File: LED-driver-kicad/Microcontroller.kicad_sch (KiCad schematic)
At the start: 11 parts, among them J2 Conn_01x05_Socket, J3 Conn_01x02_Socket, SW1 SW_SPDT, U5 PIC16F18026-ISL

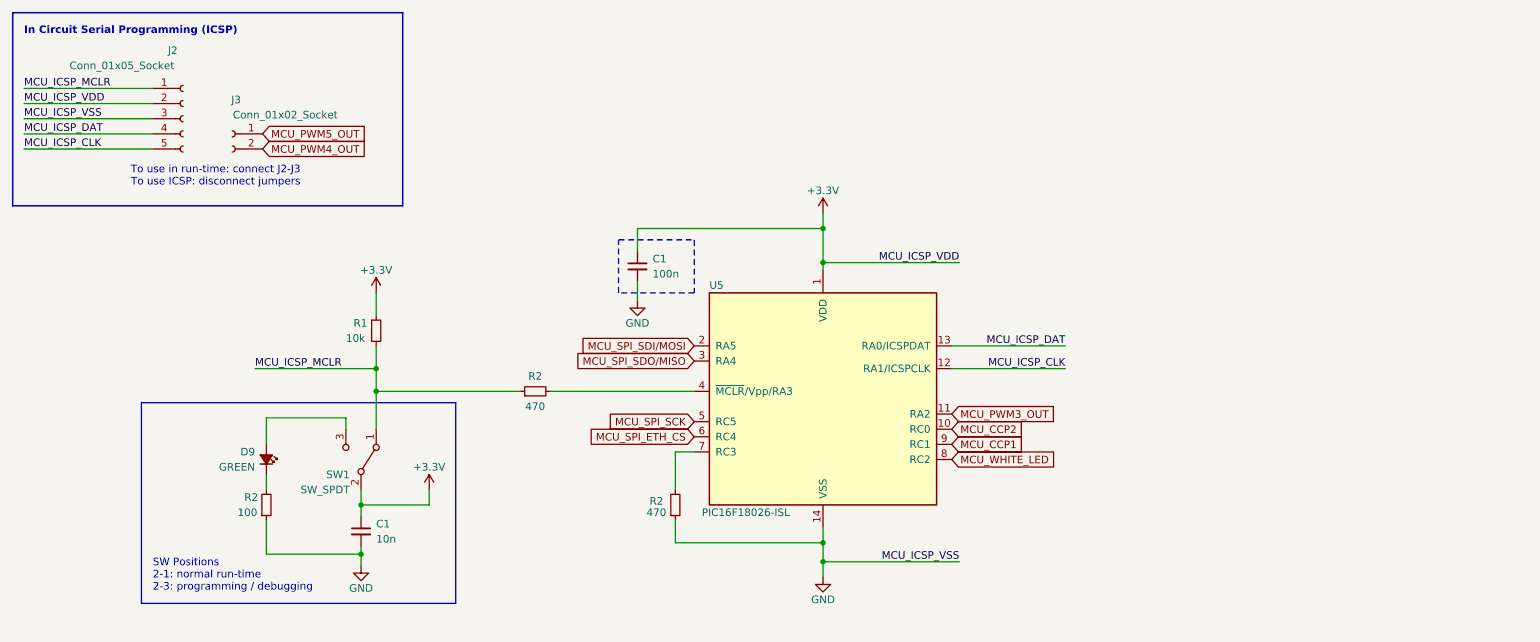
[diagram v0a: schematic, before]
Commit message: resolve Electrical Rules Checker (ERC) errors and warnings
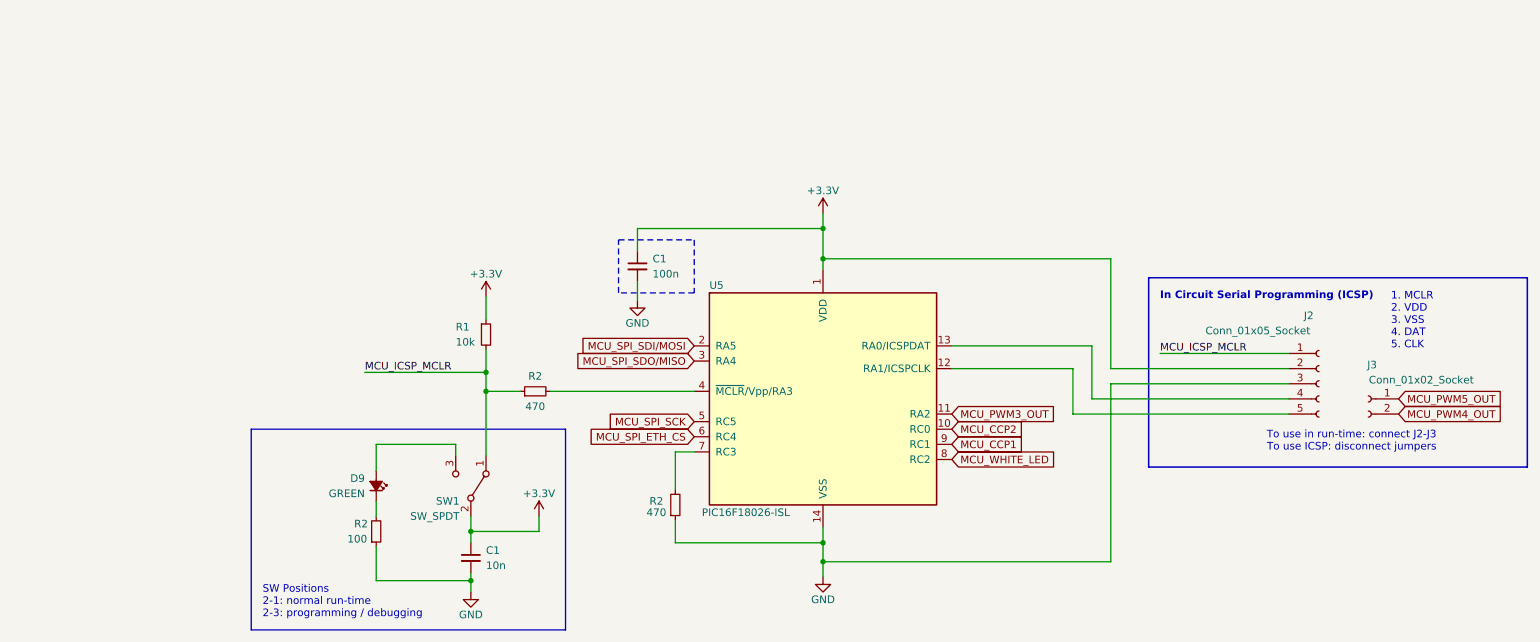
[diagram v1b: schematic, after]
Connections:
- net MCU_ICSP_CLK: no longer names the net of J2.5 (Pin_5), U5.12 (RA1/ICSPCLK)
- net MCU_ICSP_DAT: no longer names the net of J2.4 (Pin_4), U5.13 (RA0/ICSPDAT)
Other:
- note added: "1. MCLR 2. VDD 3. VSS 4. DAT 5. CLK"
- moved on the sheet: C1, D9, J2, J3, R1, R2, SW1

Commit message: update footprint assignments
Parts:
- C1: footprint (none) -> Capacitor_SMD:C_0402_1005Metric
- J2: footprint (none) -> Connector_PinSocket_1.00mm:PinSocket_1x05_P1.00mm_Vertical
- J3: footprint (none) -> Connector_PinSocket_1.00mm:PinSocket_1x02_P1.00mm_Vertical
- R1, R2: footprint (none) -> Resistor_SMD:R_0402_1005Metric
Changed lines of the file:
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@@
       (effects (font (size 1.27 1.27)))
     )
-    (property "Footprint" "" (at 80.01 106.045 0)
+    (property "Footprint" "Resistor_SMD:R_0402_1005Metric" (at 80.01 106.045 0)
       (effects (font (size 1.27 1.27)) hide)
     )
@@
       (effects (font (size 1.27 1.27)) (justify left))
     )
-    (property "Footprint" "" (at 123.825 61.595 0)
+    (property "Footprint" "Capacitor_SMD:C_0402_1005Metric" (at 123.825 61.595 0)
       (effects (font (size 1.27 1.27)) hide)
     )
@@
       (effects (font (size 1.27 1.27)))
     )
-    (property "Footprint" "" (at 106.68 82.55 0)
+    (property "Footprint" "Resistor_SMD:R_0402_1005Metric" (at 106.68 82.55 0)
       (effects (font (size 1.27 1.27)) hide)
     )
@@
       (effects (font (size 1.27 1.27)) (justify left))
     )
-    (property "Footprint" "" (at 98.425 73.025 0)
+    (property "Footprint" "Resistor_SMD:R_0402_1005Metric" (at 98.425 73.025 0)
       (effects (font (size 1.27 1.27)) hide)
     )
@@
       (effects (font (size 1.27 1.27)) (justify left))
     )
-    (property "Footprint" "" (at 238.125 81.28 0)
+    (property "Footprint" "Connector_PinSocket_1.00mm:PinSocket_1x05_P1.00mm_Vertical" (at 238.125 81.28 0)
       (effects (font (size 1.27 1.27)) hide)
     )
@@
       (effects (font (size 1.27 1.27)) (justify left))
     )
-    (property "Footprint" "" (at 95.885 110.49 0)
+    (property "Footprint" "Capacitor_SMD:C_0402_1005Metric" (at 95.885 110.49 0)
       (effects (font (size 1.27 1.27)) hide)
     )
@@
       (effects (font (size 1.27 1.27)))
     )
-    (property "Footprint" "" (at 130.175 101.6 0)
+    (property "Footprint" "Resistor_SMD:R_0402_1005Metric" (at 130.175 101.6 0)
       (effects (font (size 1.27 1.27)) hide)
     )
@@
       (effects (font (size 1.27 1.27)))
     )
-    (property "Footprint" "" (at 246.38 83.82 0)
-      (effects (font (size 1.27 1.27)) hide)
-    )
+    (property "Footprint" "Connector_PinSocket_1.00mm:PinSocket_1x02_P1.00mm_Vertical" (at 246.38 83.82 0)
+      (effects (font (size 1.27 1.27)) hide)
+    )

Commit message: update footprint assignments
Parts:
- D9: footprint (none) -> LED_SMD:LED_0603_1608Metric
- SW1: footprint (none) -> Button_Switch_THT:SW_Slide_1P2T_CK_OS102011MS2Q
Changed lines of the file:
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@@
       (effects (font (size 1.27 1.27)) (justify right))
     )
-    (property "Footprint" "" (at 95.885 98.425 0)
+    (property "Footprint" "Button_Switch_THT:SW_Slide_1P2T_CK_OS102011MS2Q" (at 95.885 98.425 0)
       (effects (font (size 1.27 1.27)) hide)
     )
@@
       (effects (font (size 1.27 1.27)) (justify right))
     )
-    (property "Footprint" "" (at 80.01 98.425 90)
+    (property "Footprint" "LED_SMD:LED_0603_1608Metric" (at 80.01 98.425 90)
       (effects (font (size 1.27 1.27)) hide)
     )

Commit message: initial PCB layout
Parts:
- SW1: footprint Button_Switch_THT:SW_Slide_1P2T_CK_OS102011MS2Q -> Button_Switch_SMD:SW_SPDT_CK-JS102011SAQN
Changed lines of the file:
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@@
       (effects (font (size 1.27 1.27)) (justify right))
     )
-    (property "Footprint" "Button_Switch_THT:SW_Slide_1P2T_CK_OS102011MS2Q" (at 95.885 98.425 0)
+    (property "Footprint" "Button_Switch_SMD:SW_SPDT_CK-JS102011SAQN" (at 95.885 98.425 0)
       (effects (font (size 1.27 1.27)) hide)
     )

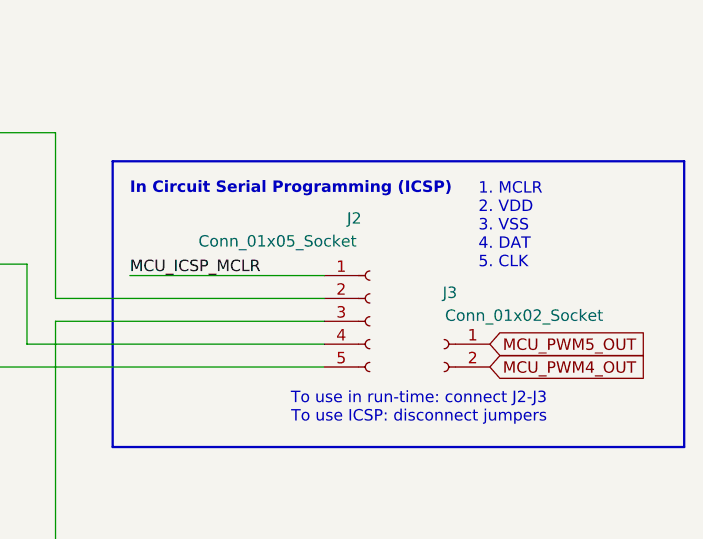
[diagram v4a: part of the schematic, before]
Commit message: add test points, net ties to schematics
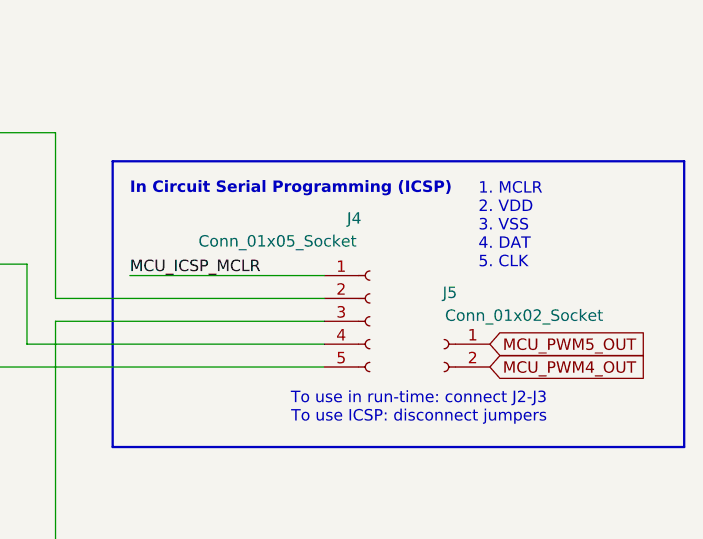
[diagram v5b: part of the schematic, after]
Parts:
- J4: renamed from J2; footprint Connector_PinSocket_1.00mm:PinSocket_1x05_P1.00mm_Vertical -> Connector_PinSocket_2.54mm:PinSocket_1x05_P2.54mm_Vertical
- J5: renamed from J3; footprint Connector_PinSocket_1.00mm:PinSocket_1x02_P1.00mm_Vertical -> Connector_PinSocket_2.54mm:PinSocket_1x02_P2.54mm_Vertical
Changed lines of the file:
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@@
         )
         (path "/2b071084-2ab6-4896-84cc-45b211479417/9127cd83-cae7-424d-ad3b-8a9e0439da28"
-          (reference "R23") (unit 1)
+          (reference "R20") (unit 1)
         )
       )
@@
         )
         (path "/2b071084-2ab6-4896-84cc-45b211479417/9127cd83-cae7-424d-ad3b-8a9e0439da28"
-          (reference "C19") (unit 1)
+          (reference "C20") (unit 1)
         )
       )
@@
         )
         (path "/2b071084-2ab6-4896-84cc-45b211479417/9127cd83-cae7-424d-ad3b-8a9e0439da28"
-          (reference "#PWR032") (unit 1)
+          (reference "#PWR026") (unit 1)
         )
       )
@@
   (symbol (lib_id "power:GND") (at 154.94 113.665 0) (unit 1)
     (in_bom yes) (on_board yes) (dnp no)
-    (property "Reference" "#PWR033" (at 154.94 120.015 0)
+    (property "Reference" "#PWR031" (at 154.94 120.015 0)
       (effects (font (size 1.27 1.27)) hide)
     )
@@
       (project "LED-driver-kicad"
         (path "/2b071084-2ab6-4896-84cc-45b211479417/9127cd83-cae7-424d-ad3b-8a9e0439da28"
-          (reference "#PWR033") (unit 1)
+          (reference "#PWR031") (unit 1)
         )
       )
@@
         )
         (path "/2b071084-2ab6-4896-84cc-45b211479417/9127cd83-cae7-424d-ad3b-8a9e0439da28"
-          (reference "#PWR031") (unit 1)
+          (reference "#PWR028") (unit 1)
         )
       )
@@
   (symbol (lib_id "power:GND") (at 123.825 67.31 0) (unit 1)
     (in_bom yes) (on_board yes) (dnp no)
-    (property "Reference" "#PWR030" (at 123.825 73.66 0)
+    (property "Reference" "#PWR029" (at 123.825 73.66 0)
       (effects (font (size 1.27 1.27)) hide)
     )
@@
       (project "LED-driver-kicad"
         (path "/2b071084-2ab6-4896-84cc-45b211479417/9127cd83-cae7-424d-ad3b-8a9e0439da28"
-          (reference "#PWR030") (unit 1)
+          (reference "#PWR029") (unit 1)
         )
       )
@@
   (symbol (lib_id "Connector:Conn_01x05_Socket") (at 238.125 81.28 0) (unit 1)
     (in_bom yes) (on_board yes) (dnp no)
-    (property "Reference" "J2" (at 235.585 69.85 0)
+    (property "Reference" "J4" (at 235.585 69.85 0)
       (effects (font (size 1.27 1.27)) (justify left))
     )
@@
       (effects (font (size 1.27 1.27)) (justify left))
     )
-    (property "Footprint" "Connector_PinSocket_1.00mm:PinSocket_1x05_P1.00mm_Vertical" (at 238.125 81.28 0)
+    (property "Footprint" "Connector_PinSocket_2.54mm:PinSocket_1x05_P2.54mm_Vertical" (at 238.125 81.28 0)
       (effects (font (size 1.27 1.27)) hide)
     )
@@
       (project "LED-driver-kicad"
         (path "/2b071084-2ab6-4896-84cc-45b211479417/9127cd83-cae7-424d-ad3b-8a9e0439da28"
-          (reference "J2") (unit 1)
+          (reference "J4") (unit 1)
         )
       )
@@
         )
         (path "/2b071084-2ab6-4896-84cc-45b211479417/9127cd83-cae7-424d-ad3b-8a9e0439da28"
-          (reference "C20") (unit 1)
+          (reference "C19") (unit 1)
         )
       )
@@
         )
         (path "/2b071084-2ab6-4896-84cc-45b211479417/9127cd83-cae7-424d-ad3b-8a9e0439da28"
-          (reference "#PWR029") (unit 1)
+          (reference "#PWR027") (unit 1)
         )
       )
@@
         )
         (path "/2b071084-2ab6-4896-84cc-45b211479417/9127cd83-cae7-424d-ad3b-8a9e0439da28"
-          (reference "R24") (unit 1)
+          (reference "R23") (unit 1)
         )
       )
@@
   (symbol (lib_id "Connector:Conn_01x02_Socket") (at 246.38 83.82 0) (mirror y) (unit 1)
     (in_bom yes) (on_board yes) (dnp no)
-    (property "Reference" "J3" (at 247.015 78.105 0)
+    (property "Reference" "J5" (at 247.015 78.105 0)
       (effects (font (size 1.27 1.27)))
     )
@@
       (effects (font (size 1.27 1.27)))
     )
-    (property "Footprint" "Connector_PinSocket_1.00mm:PinSocket_1x02_P1.00mm_Vertical" (at 246.38 83.82 0)
+    (property "Footprint" "Connector_PinSocket_2.54mm:PinSocket_1x02_P2.54mm_Vertical" (at 246.38 83.82 0)
       (effects (font (size 1.27 1.27)) hide)
     )
@@
       (project "LED-driver-kicad"
         (path "/2b071084-2ab6-4896-84cc-45b211479417/9127cd83-cae7-424d-ad3b-8a9e0439da28"
-          (reference "J3") (unit 1)
+          (reference "J5") (unit 1)
         )
       )
@@
   (symbol (lib_id "power:+3.3V") (at 154.94 52.705 0) (unit 1)
     (in_bom yes) (on_board yes) (dnp no)
-    (property "Reference" "#PWR028" (at 154.94 56.515 0)
+    (property "Reference" "#PWR030" (at 154.94 56.515 0)
       (effects (font (size 1.27 1.27)) hide)
     )
@@
       (project "LED-driver-kicad"
         (path "/2b071084-2ab6-4896-84cc-45b211479417/9127cd83-cae7-424d-ad3b-8a9e0439da28"
-          (reference "#PWR028") (unit 1)
-        )
-      )
+          (reference "#PWR030") (unit 1)
+        )
+      )
